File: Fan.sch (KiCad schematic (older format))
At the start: 0 parts

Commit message: Fan Module details
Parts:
- added Q?: MOSFET_N, ~, symbol MOSFET_N
- added R? (x5): R, ~, symbol R
- added RV?: POT, ~, symbol POT
- added U?: LM324, symbol LM324
- added U?: MCP4922-E/P, DIP14, symbol MCP4922-E/P
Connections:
- net labels added: +12V, -12V, AGND, CS_N, Current_Measure, MISO, MOSI, SCLK
- wire segments 0 -> 33

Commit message: Arduino Modules
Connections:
- net labels added: CURR_MEAS, FAN_EN_N, FAN_OUT+, FAN_OUT-, TACH_IN, TACH_MEAS
- net labels removed: Current_Measure, Fan_In, Power+, Power-, Tach, Tach_out
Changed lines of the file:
@@
 Sheet 6 9
 Title ""
-Date "22 may 2014"
+Date "24 may 2014"
 Rev ""
 Comp ""
@@
 $EndDescr
 Text HLabel 10350 3250 0    60   Output ~ 0
-Power+
-Text HLabel 10350 3600 0    60   Input ~ 0
-Power-
+FAN_OUT+
+Text HLabel 10350 3600 0    60   Output ~ 0
+FAN_OUT-
 Text HLabel 10300 4200 0    60   Input ~ 0
-Tach
+TACH_IN
 Text HLabel 1300 4750 0    60   Output ~ 0
-Tach_out
+TACH_MEAS
 Text HLabel 1250 3900 0    60   Input ~ 0
-Fan_In
+FAN_EN_N
 $Comp
 L MOSFET_N Q?
@@
 $EndComp
 Text HLabel 1350 4500 0    60   Output ~ 0
-Current_Measure
+CURR_MEAS
 Wire Wire Line
 	7650 1900 7650 2500

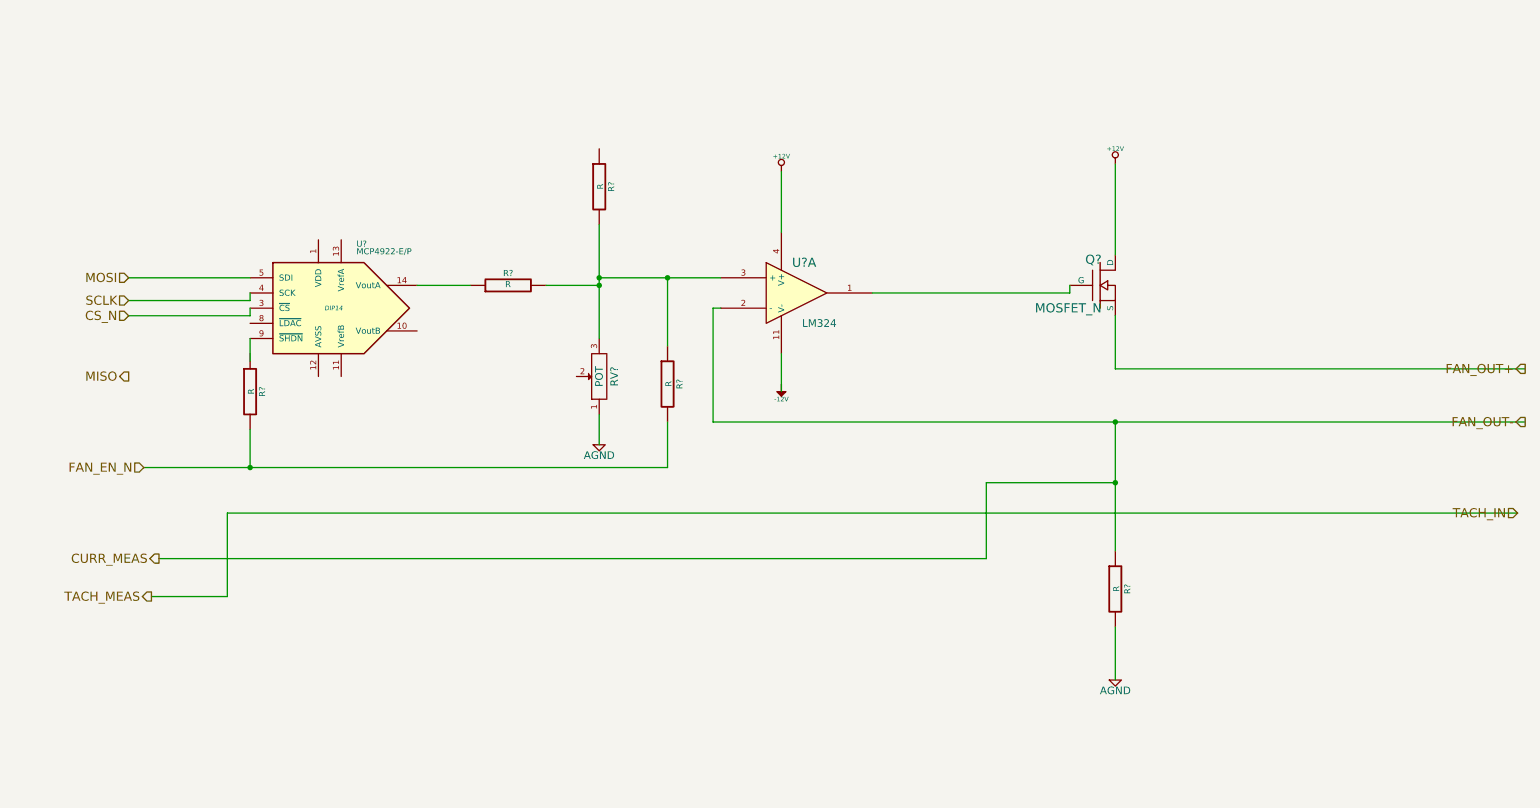
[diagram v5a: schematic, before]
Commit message: Fan/Current Module Refactoring
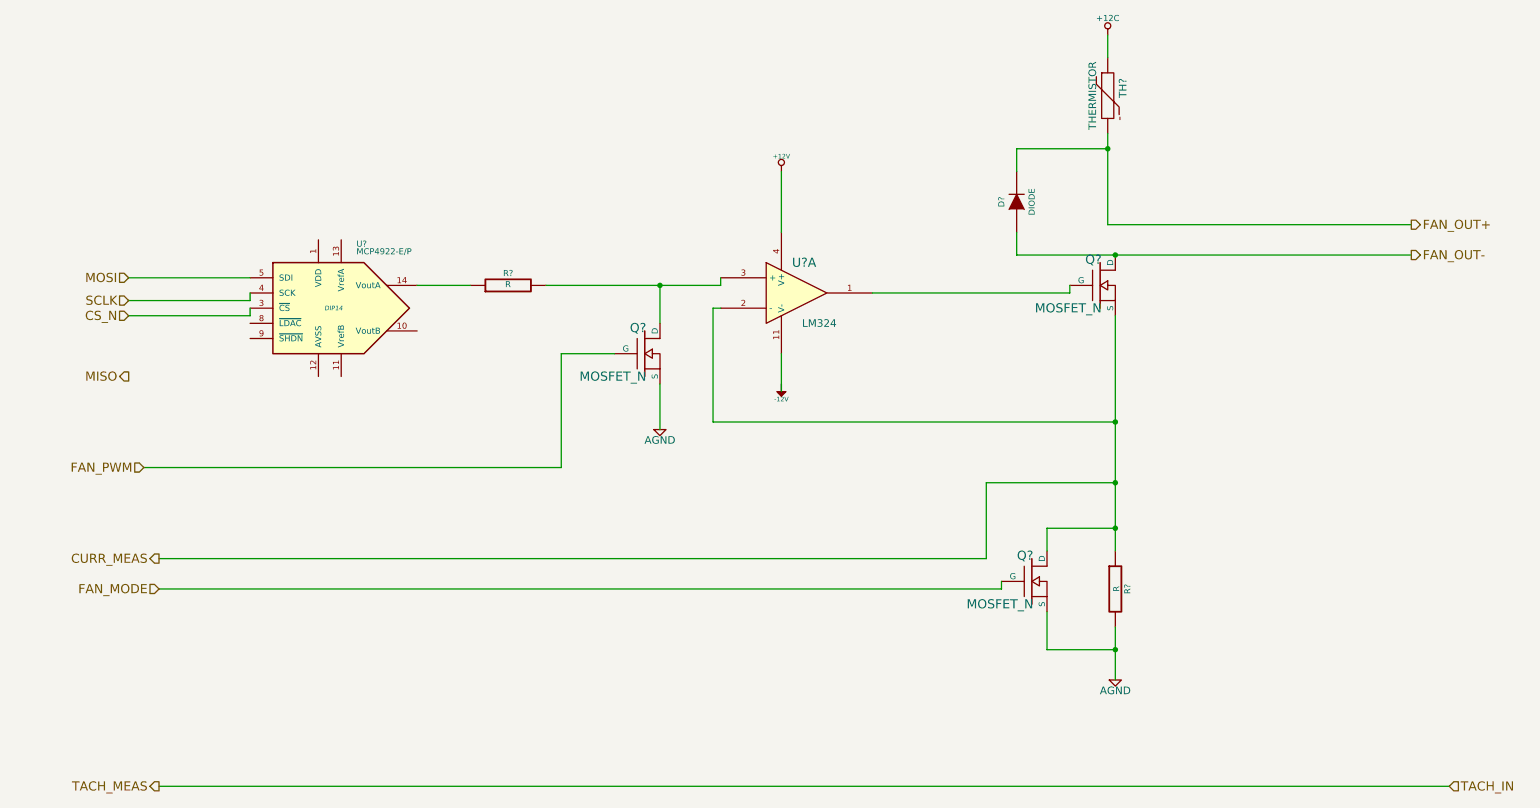
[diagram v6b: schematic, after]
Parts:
- removed R? (x3): R, ~, symbol R
- removed RV?: POT, ~, symbol POT
- added D?: DIODE, ~, symbol DIODE
- added Q? (x2): MOSFET_N, ~, symbol MOSFET_N
- added TH?: THERMISTOR, ~, symbol THERMISTOR
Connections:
- net labels added: +12C, FAN_MODE, FAN_PWM
- net labels removed: FAN_EN_N
- wire segments 33 -> 39
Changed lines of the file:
@@
 Sheet 6 9
 Title ""
-Date "24 may 2014"
+Date "25 may 2014"
 Rev ""
 Comp ""
@@
 Comment4 ""
 $EndDescr
-Text HLabel 10350 3250 0    60   Output ~ 0
+Text HLabel 9600 2300 2    60   Output ~ 0
 FAN_OUT+
-Text HLabel 10350 3600 0    60   Output ~ 0
+Text HLabel 9600 2500 2    60   Output ~ 0
 FAN_OUT-
-Text HLabel 10300 4200 0    60   Input ~ 0
+Text HLabel 9850 6000 2    60   Input ~ 0
 TACH_IN
-Text HLabel 1300 4750 0    60   Output ~ 0
+Text HLabel 1350 6000 0    60   Output ~ 0
 TACH_MEAS
 Text HLabel 1250 3900 0    60   Input ~ 0
-FAN_EN_N
+FAN_PWM
 $Comp
 L MOSFET_N Q?
@@
 F 3 "" H 5550 2750 60  0000 C CNN
 	1    5550 2750
-	1    0    0    -1
-$EndComp
-$Comp
-L +12V #PWR?
-U 1 1 537CE0A7
-P 7650 1900
-F 0 "#PWR?" H 7650 1850 20  0001 C CNN
-F 1 "+12V" H 7650 2000 30  0000 C CNN
-F 2 "" H 7650 1900 60  0000 C CNN
-F 3 "" H 7650 1900 60  0000 C CNN
-	1    7650 1900
 	1    0    0    -1
 $EndComp
@@
 $EndComp
 $Comp
-L R R?
-U 1 1 537CE89E
-P 4250 2050
-F 0 "R?" V 4330 2050 40  0000 C CNN
-F 1 "R" V 4257 2051 40  0000 C CNN
-F 2 "~" V 4180 2050 30  0000 C CNN
-F 3 "~" H 4250 2050 30  0000 C CNN
-	1    4250 2050
-	1    0    0    -1
-$EndComp
-$Comp
-L POT RV?
-U 1 1 537CE8C3
-P 4250 3300
-F 0 "RV?" H 4250 3200 50  0000 C CNN
-F 1 "POT" H 4250 3300 50  0000 C CNN
-F 2 "~" H 4250 3300 60  0000 C CNN
-F 3 "~" H 4250 3300 60  0000 C CNN
-	1    4250 3300
-	0    -1   -1   0
-$EndComp
-$Comp
 L AGND #PWR?
 U 1 1 537CEA45
-P 4250 3750
-F 0 "#PWR?" H 4250 3750 40  0001 C CNN
-F 1 "AGND" H 4250 3680 50  0000 C CNN
-F 2 "" H 4250 3750 60  0000 C CNN
-F 3 "" H 4250 3750 60  0000 C CNN
-	1    4250 3750
+P 4650 3650
+F 0 "#PWR?" H 4650 3650 40  0001 C CNN
+F 1 "AGND" H 4650 3580 50  0000 C CNN
+F 2 "" H 4650 3650 60  0000 C CNN
+F 3 "" H 4650 3650 60  0000 C CNN
+	1    4650 3650
 	1    0    0    -1
 $EndComp
@@
 Text HLabel 1350 4500 0    60   Output ~ 0
 CURR_MEAS
-Wire Wire Line
-	7650 1900 7650 2500
-Wire Wire Line
-	6050 2750 7350 2750
-Wire Wire Line
-	7350 2750 7350 2700
-Wire Wire Line
-	7650 2900 7650 3250
-Wire Wire Line
-	7650 3250 10350 3250
-Wire Wire Line
-	5450 3150 5450 3400
-Wire Wire Line
-	5450 2350 5450 1950
-Wire Wire Line
-	5050 2850 5000 2850
-Wire Wire Line
-	5000 2850 5000 3600
-Wire Wire Line
-	5000 3600 10350 3600
-Wire Wire Line
-	7650 3600 7650 4450
-Connection ~ 7650 3600
-Wire Wire Line
-	7650 4950 7650 5300
-Wire Wire Line
-	4250 2300 4250 3050
-Wire Wire Line
-	5050 2650 4250 2650
-Connection ~ 4250 2650
-Wire Wire Line
-	4250 3550 4250 3750
-Wire Wire Line
-	10300 4200 1800 4200
-Wire Wire Line
-	1800 4200 1800 4750
-Wire Wire Line
-	1800 4750 1300 4750
-Wire Wire Line
-	1350 4500 6800 4500
-Wire Wire Line
-	6800 4500 6800 4000
-Wire Wire Line
-	6800 4000 7650 4000
-Connection ~ 7650 4000
-$Comp
-L R R?
-U 1 1 537CF378
-P 4700 3350
-F 0 "R?" V 4780 3350 40  0000 C CNN
-F 1 "R" V 4707 3351 40  0000 C CNN
-F 2 "~" V 4630 3350 30  0000 C CNN
-F 3 "~" H 4700 3350 30  0000 C CNN
-	1    4700 3350
-	1    0    0    -1
-$EndComp
-Wire Wire Line
-	4700 2650 4700 3100
-Connection ~ 4700 2650
-Wire Wire Line
-	1250 3900 4700 3900
-Wire Wire Line
-	4700 3900 4700 3600
 $Comp
 L R R?
@@
 	0    -1   -1   0
 $EndComp
-Wire Wire Line
-	3050 2700 3400 2700
-Wire Wire Line
-	3900 2700 4250 2700
-Connection ~ 4250 2700
 Text HLabel 1150 2650 0    60   Input ~ 0
 MOSI
@@
 Text HLabel 1150 2800 0    60   Input ~ 0
 SCLK
+$Comp
+L MOSFET_N Q?
+U 1 1 53813A87
+P 7100 4650
+F 0 "Q?" H 7110 4820 60  0000 R CNN
+F 1 "MOSFET_N" H 7110 4500 60  0000 R CNN
+F 2 "~" H 7100 4650 60  0000 C CNN
+F 3 "~" H 7100 4650 60  0000 C CNN
+	1    7100 4650
+	1    0    0    -1
+$EndComp
+$Comp
+L THERMISTOR TH?
+U 1 1 53813A9E
+P 7600 1450
+F 0 "TH?" V 7700 1500 50  0000 C CNN
+F 1 "THERMISTOR" V 7500 1450 50  0000 C CNN
+F 2 "~" H 7600 1450 60  0000 C CNN
+F 3 "~" H 7600 1450 60  0000 C CNN
+	1    7600 1450
+	1    0    0    -1
+$EndComp
+$Comp
+L DIODE D?
+U 1 1 53814493
+P 7000 2150
+F 0 "D?" H 7000 2250 40  0000 C CNN
+F 1 "DIODE" H 7000 2050 40  0000 C CNN
+F 2 "~" H 7000 2150 60  0000 C CNN
+F 3 "~" H 7000 2150 60  0000 C CNN
+	1    7000 2150
+	0    -1   -1   0
+$EndComp
+Wire Wire Line
+	6050 2750 7350 2750
+Wire Wire Line
+	7350 2750 7350 2700
+Wire Wire Line
+	5450 3150 5450 3400
+Wire Wire Line
+	5450 2350 5450 1950
+Wire Wire Line
+	5050 2850 5000 2850
+Wire Wire Line
+	5000 2850 5000 3600
+Wire Wire Line
+	7650 2900 7650 4450
+Connection ~ 7650 3600
+Wire Wire Line
+	7650 4950 7650 5300
+Wire Wire Line
+	1350 4500 6800 4500
+Wire Wire Line
+	6800 4500 6800 4000
+Wire Wire Line
+	6800 4000 7650 4000
+Connection ~ 7650 4000
+Wire Wire Line
+	3050 2700 3400 2700
 Wire Wire Line
 	1150 2650 1950 2650
@@
 Wire Wire Line
 	1950 2900 1950 2850
-$Comp
-L R R?
-U 1 1 537CFA87
-P 1950 3400
-F 0 "R?" V 2030 3400 40  0000 C CNN
-F 1 "R" V 1957 3401 40  0000 C CNN
-F 2 "~" V 1880 3400 30  0000 C CNN
-F 3 "~" H 1950 3400 30  0000 C CNN
-	1    1950 3400
-	1    0    0    -1
-$EndComp
-Wire Wire Line
-	1950 3050 1950 3200
-Wire Wire Line
-	1950 3650 1950 3900
-Connection ~ 1950 3900
+Wire Wire Line
+	7000 2500 9600 2500
+Connection ~ 7650 2500
+Wire Wire Line
+	5000 3600 7650 3600
+Wire Wire Line
+	7200 4450 7200 4300
+Wire Wire Line
+	7200 4300 7650 4300
+Connection ~ 7650 4300
+Wire Wire Line
+	7200 4850 7200 5100
+Wire Wire Line
+	7200 5100 7650 5100
+Connection ~ 7650 5100
+Wire Wire Line
+	1350 6000 9850 6000
+Wire Wire Line
+	3900 2700 5050 2700
+Wire Wire Line
+	5050 2700 5050 2650
+$Comp
+L MOSFET_N Q?
+U 1 1 53814FC1
+P 4550 3150
+F 0 "Q?" H 4560 3320 60  0000 R CNN
+F 1 "MOSFET_N" H 4560 3000 60  0000 R CNN
+F 2 "~" H 4550 3150 60  0000 C CNN
+F 3 "~" H 4550 3150 60  0000 C CNN
+	1    4550 3150
+	1    0    0    -1
+$EndComp
+Wire Wire Line
+	4650 3350 4650 3650
+Wire Wire Line
+	1250 3900 4000 3900
+Wire Wire Line
+	4000 3900 4000 3150
+Wire Wire Line
+	4000 3150 4350 3150
+Wire Wire Line
+	4650 2950 4650 2700
+Connection ~ 4650 2700
+Text HLabel 1350 4700 0    60   Input ~ 0
+FAN_MODE
+Wire Wire Line
+	1350 4700 6900 4700
+Wire Wire Line
+	6900 4700 6900 4650
+$Comp
+L +12C #PWR?
+U 1 1 53816261
+P 7600 1050
+F 0 "#PWR?" H 7600 1020 30  0001 C CNN
+F 1 "+12C" H 7600 1160 40  0000 C CNN
+F 2 "" H 7600 1050 60  0000 C CNN
+F 3 "" H 7600 1050 60  0000 C CNN
+	1    7600 1050
+	1    0    0    -1
+$EndComp
+Wire Wire Line
+	7600 1700 7600 2300
+Wire Wire Line
+	7600 2300 9600 2300
+Wire Wire Line
+	7600 1050 7600 1200
+Wire Wire Line
+	7000 1950 7000 1800
+Wire Wire Line
+	7000 1800 7600 1800
+Connection ~ 7600 1800
+Wire Wire Line
+	7000 2350 7000 2500
 $EndSCHEMATC
